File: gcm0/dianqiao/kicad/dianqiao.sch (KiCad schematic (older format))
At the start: 85 parts, among them J1 Conn_Coaxial, J2 Conn_Coaxial, J3 Conn_Coaxial, J4 Conn_Coaxial, SW1 2, SW2 0, SW3 1, U1 NE5532, U10 TL084, U11 NE5532, U12 NE5532, U2 LM2596T-ADJ, U3 LM1117-3.3, U4 LM7805_TO220, U5 STM32F030F4P6, U6 CD4052B, U7 NE5532, U8 CD4053B, U9 74HC595, Y1 8M

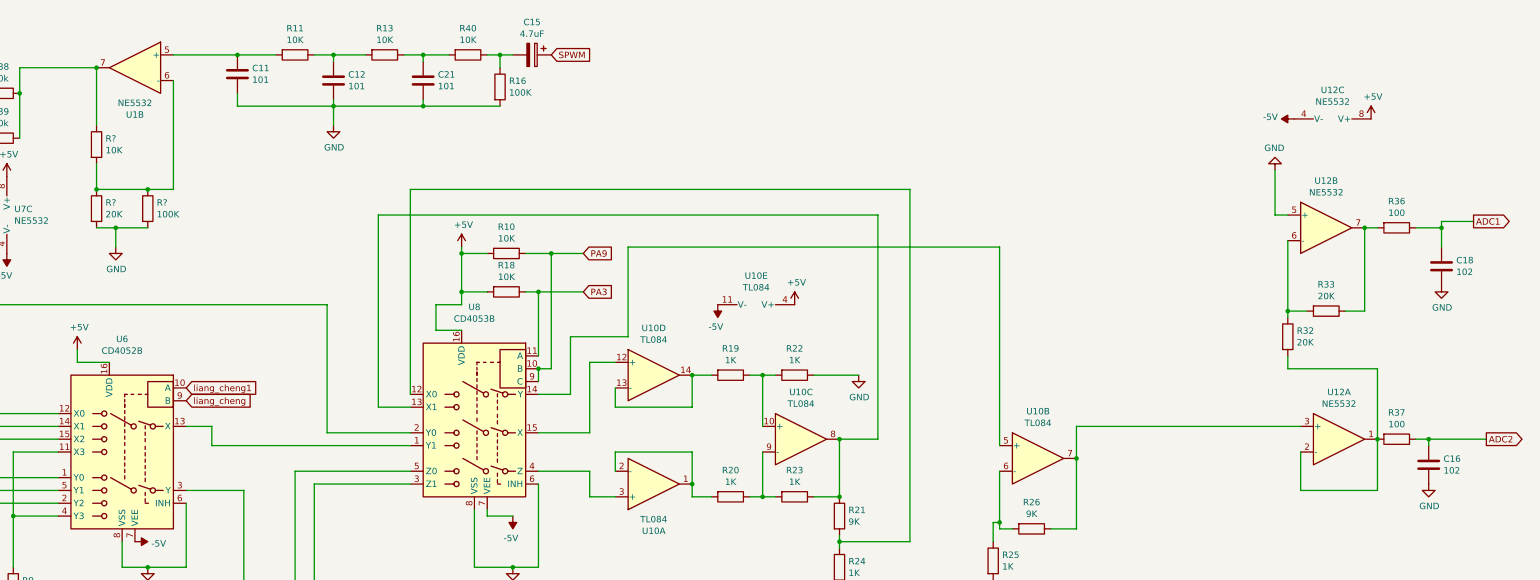
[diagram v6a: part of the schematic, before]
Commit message: 自动量程成功
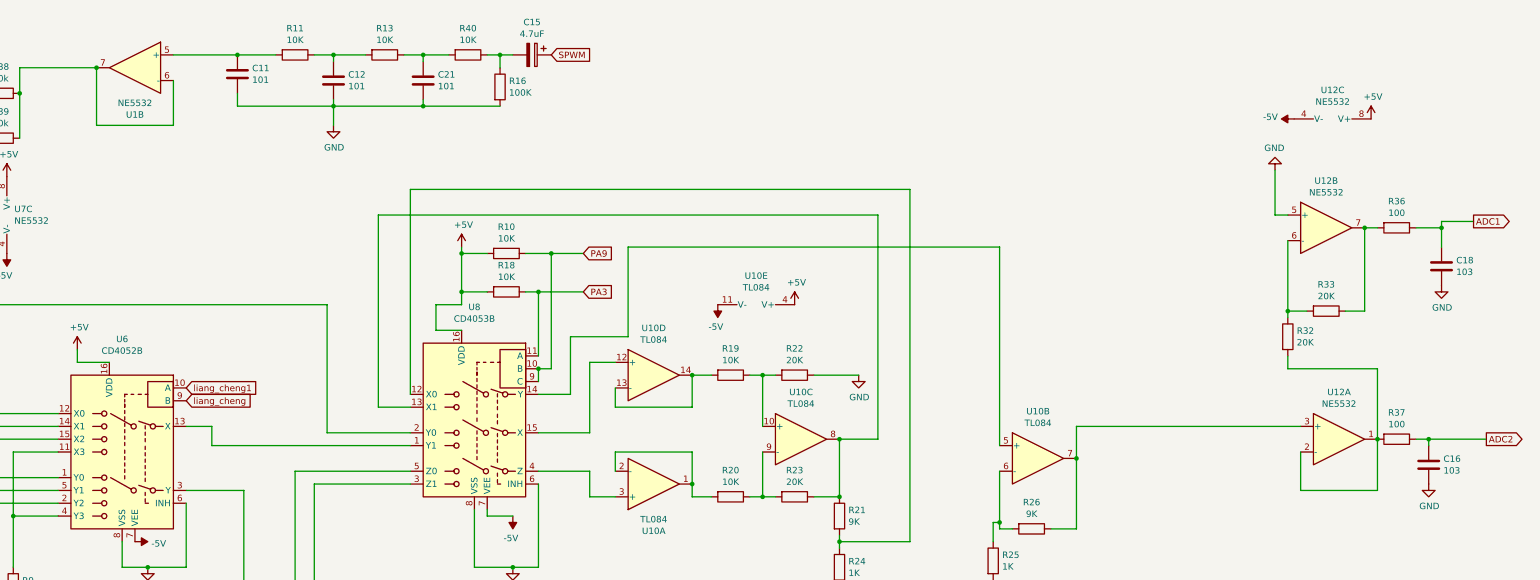
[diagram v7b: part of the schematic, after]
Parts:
- removed R?: 10K, symbol Device:R
- removed R?: 20K, symbol Device:R
- removed R?: 100K, symbol Device:R
- C16, C18: value 102 -> 103
- R19, R20: value 1K -> 10K
- R22, R23: value 1K -> 20K
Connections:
- net at R38.1, R39.1, U1.7: now also U1.6 (-)
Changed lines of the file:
@@
 P 9800 3400
 F 0 "R19" V 9593 3400 50  0000 C CNN
-F 1 "1K" V 9684 3400 50  0000 C CNN
+F 1 "10K" V 9684 3400 50  0000 C CNN
 F 2 "" V 9730 3400 50  0001 C CNN
 F 3 "~" H 9800 3400 50  0001 C CNN
@@
 P 10300 3400
 F 0 "R22" V 10093 3400 50  0000 C CNN
-F 1 "1K" V 10184 3400 50  0000 C CNN
+F 1 "20K" V 10184 3400 50  0000 C CNN
 F 2 "" V 10230 3400 50  0001 C CNN
 F 3 "~" H 10300 3400 50  0001 C CNN
@@
 P 9800 4350
 F 0 "R20" V 9593 4350 50  0000 C CNN
-F 1 "1K" V 9684 4350 50  0000 C CNN
+F 1 "10K" V 9684 4350 50  0000 C CNN
 F 2 "" V 9730 4350 50  0001 C CNN
 F 3 "~" H 9800 4350 50  0001 C CNN
@@
 P 10300 4350
 F 0 "R23" V 10093 4350 50  0000 C CNN
-F 1 "1K" V 10184 4350 50  0000 C CNN
+F 1 "20K" V 10184 4350 50  0000 C CNN
 F 2 "" V 10230 4350 50  0001 C CNN
 F 3 "~" H 10300 4350 50  0001 C CNN
@@
 P 15350 2550
 F 0 "C18" H 15465 2596 50  0000 L CNN
-F 1 "102" H 15465 2505 50  0000 L CNN
+F 1 "103" H 15465 2505 50  0000 L CNN
 F 2 "" H 15388 2400 50  0001 C CNN
 F 3 "~" H 15350 2550 50  0001 C CNN
@@
 P 15250 4100
 F 0 "C16" H 15365 4146 50  0000 L CNN
-F 1 "102" H 15365 4055 50  0000 L CNN
+F 1 "103" H 15365 4055 50  0000 L CNN
 F 2 "" H 15288 3950 50  0001 C CNN
 F 3 "~" H 15250 4100 50  0001 C CNN
@@
 Wire Wire Line
 	3000 1200 3000 1700
-$Comp
-L Device:R R?
-U 1 1 5F481BA7
-P 4850 1600
-F 0 "R?" H 4920 1646 50  0000 L CNN
-F 1 "10K" H 4920 1555 50  0000 L CNN
-F 2 "" V 4780 1600 50  0001 C CNN
-F 3 "~" H 4850 1600 50  0001 C CNN
-	1    4850 1600
-	1    0    0    -1
-$EndComp
-$Comp
-L Device:R R?
-U 1 1 5F48359F
-P 4850 2100
-F 0 "R?" H 4920 2146 50  0000 L CNN
-F 1 "20K" H 4920 2055 50  0000 L CNN
-F 2 "" V 4780 2100 50  0001 C CNN
-F 3 "~" H 4850 2100 50  0001 C CNN
-	1    4850 2100
-	1    0    0    -1
-$EndComp
-$Comp
-L Device:R R?
-U 1 1 5F484BA7
-P 5250 2100
-F 0 "R?" H 5320 2146 50  0000 L CNN
-F 1 "100K" H 5320 2055 50  0000 L CNN
-F 2 "" V 5180 2100 50  0001 C CNN
-F 3 "~" H 5250 2100 50  0001 C CNN
-	1    5250 2100
-	1    0    0    -1
-$EndComp
-Wire Wire Line
-	5250 1950 4850 1950
-Wire Wire Line
-	4850 1750 4850 1950
-Connection ~ 4850 1950
 Wire Wire Line
 	4850 1450 4850 1000
 Connection ~ 4850 1000
 Wire Wire Line
-	5250 2250 5000 2250
-$Comp
-L power:GND #PWR?
-U 1 1 5F51CD3A
-P 5000 2400
-F 0 "#PWR?" H 5000 2150 50  0001 C CNN
-F 1 "GND" H 5005 2227 50  0000 C CNN
-F 2 "" H 5000 2400 50  0001 C CNN
-F 3 "" H 5000 2400 50  0001 C CNN
-	1    5000 2400
-	1    0    0    -1
-$EndComp
-Wire Wire Line
-	5000 2400 5000 2250
-Connection ~ 5000 2250
-Wire Wire Line
-	5000 2250 4850 2250
-Wire Wire Line
-	5450 1100 5450 1950
-Wire Wire Line
-	5450 1950 5250 1950
-Connection ~ 5250 1950
+	5450 1100 5450 1450
+Wire Wire Line
+	5450 1450 4850 1450
 $EndSCHEMATC

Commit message: 显示上下臂
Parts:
- added R? (x2): 10K, symbol Device:R
- R19, R20: value 10K -> 20K
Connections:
- net GND: now also R?.2
- net at R38.1, R39.1, U1.7: now also R?.1; no longer U1.6 (-)
- new net: R?.1, R?.2, U1.6 (-)
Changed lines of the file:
@@
 P 9800 3400
 F 0 "R19" V 9593 3400 50  0000 C CNN
-F 1 "10K" V 9684 3400 50  0000 C CNN
+F 1 "20K" V 9684 3400 50  0000 C CNN
 F 2 "" V 9730 3400 50  0001 C CNN
 F 3 "~" H 9800 3400 50  0001 C CNN
@@
 P 9800 4350
 F 0 "R20" V 9593 4350 50  0000 C CNN
-F 1 "10K" V 9684 4350 50  0000 C CNN
+F 1 "20K" V 9684 4350 50  0000 C CNN
 F 2 "" V 9730 4350 50  0001 C CNN
 F 3 "~" H 9800 4350 50  0001 C CNN
@@
 Wire Wire Line
 	3000 1200 3000 1700
-Wire Wire Line
-	4850 1450 4850 1000
 Connection ~ 4850 1000
-Wire Wire Line
-	5450 1100 5450 1450
-Wire Wire Line
-	5450 1450 4850 1450
+$Comp
+L Device:R R?
+U 1 1 5F4D0F44
+P 4850 1700
+F 0 "R?" H 4920 1746 50  0000 L CNN
+F 1 "10K" H 4920 1655 50  0000 L CNN
+F 2 "" V 4780 1700 50  0001 C CNN
+F 3 "~" H 4850 1700 50  0001 C CNN
+	1    4850 1700
+	1    0    0    -1
+$EndComp
+$Comp
+L Device:R R?
+U 1 1 5F4D292C
+P 4850 2100
+F 0 "R?" H 4920 2146 50  0000 L CNN
+F 1 "10K" H 4920 2055 50  0000 L CNN
+F 2 "" V 4780 2100 50  0001 C CNN
+F 3 "~" H 4850 2100 50  0001 C CNN
+	1    4850 2100
+	1    0    0    -1
+$EndComp
+$Comp
+L power:GND #PWR?
+U 1 1 5F4D4346
+P 4850 2250
+F 0 "#PWR?" H 4850 2000 50  0001 C CNN
+F 1 "GND" H 4855 2077 50  0000 C CNN
+F 2 "" H 4850 2250 50  0001 C CNN
+F 3 "" H 4850 2250 50  0001 C CNN
+	1    4850 2250
+	1    0    0    -1
+$EndComp
+Wire Wire Line
+	4850 1000 4850 1550
+Wire Wire Line
+	4850 1850 4850 1900
+Wire Wire Line
+	5450 1900 4850 1900
+Wire Wire Line
+	5450 1100 5450 1900
+Connection ~ 4850 1900
+Wire Wire Line
+	4850 1900 4850 1950
 $EndSCHEMATC
